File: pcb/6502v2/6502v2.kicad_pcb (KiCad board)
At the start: 2 copper layers, 119 x 119 mm, 89 parts, among them J1 Power, J10 Interup Pins, J11 I/O, J12 DB9_Female, J2 USB_C_Receptacle, J3 Barrel_Jack, J4 Conn_01x02, J5 I/O, J6 Interup Pins, J7 I/O, J8 I/O, J9 LDC, SW2 SW_Push, U1 74HC00, U2 74HC238, U3 CY62256-70PC, U4 W65C02SxP, U5 W65C22NxP, U6 W65C22NxP, U7 MAX232, U8 W65C51NxP, U9 28C256, X1 DGOF5S3, Y1 1.8432 Mh

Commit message: Laying out chips
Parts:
- moved R33 101.1 mm to (75.5, 48.0)
- moved C5 97.5 mm to (68.0, 52.0), turned to 90 degrees
- moved U2 89.4 mm to (165.4, 103.8)
- moved J6 59.7 mm to (122.4, 103.4), turned to 90 degrees
- moved U4 51.1 mm to (71.9, 107.1), turned to 180 degrees
- moved U5 49.2 mm to (134.2, 99.9), turned to 180 degrees
- moved J1 42.5 mm to (20.7, 149.6)
- moved J5 35.2 mm to (139.7, 94.5), turned to 180 degrees
- moved Y1 33.5 mm to (77.7, 52.0)
- moved U7 28.4 mm to (57.5, 47.4)
- moved J11 28.1 mm to (159.4, 88.4), turned to 180 degrees
- moved J12 24.0 mm to (45.3, 47.8)
- moved J10 20.2 mm to (151.2, 127.0)
- moved J8 16.8 mm to (153.0, 83.2), turned to 180 degrees
- moved J7 15.9 mm to (139.8, 73.3), turned to 180 degrees
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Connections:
- U2 pad 11: /Serial ~{Enable} -> /Serial Enable
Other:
- board size 119 x 119 mm -> 109 x 119 mm

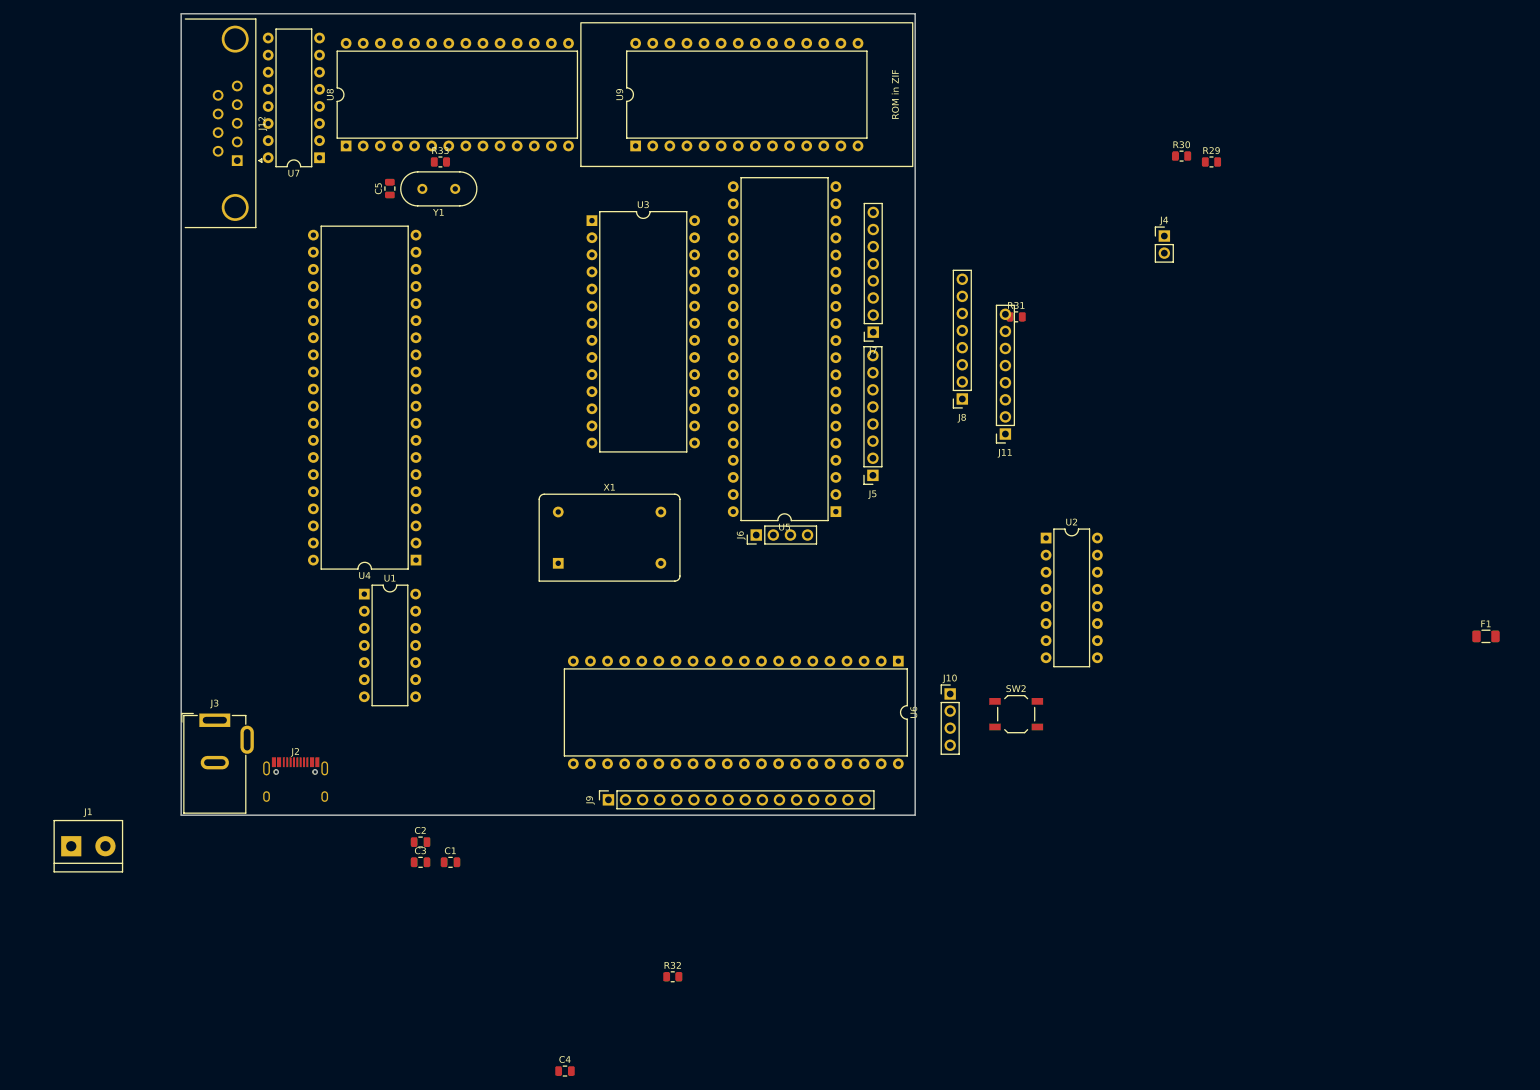
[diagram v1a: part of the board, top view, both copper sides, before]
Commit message: Yo yo yo i make the bord 102 by 102 cause jlc pricing
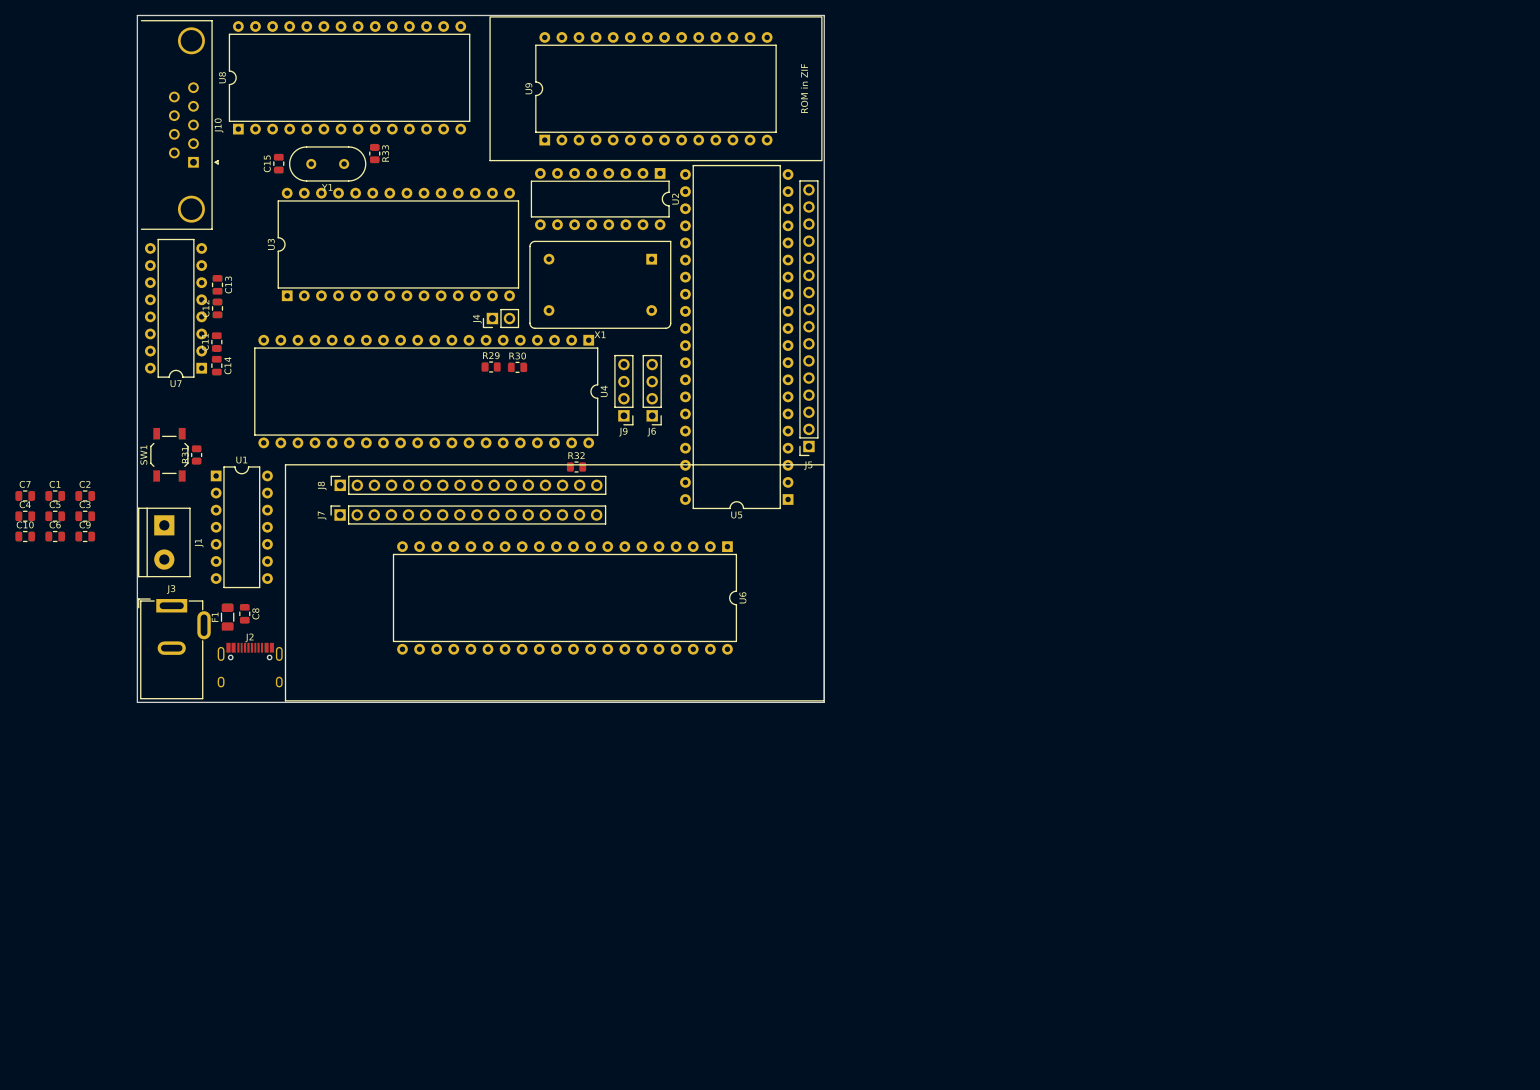
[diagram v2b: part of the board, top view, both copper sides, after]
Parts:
- removed J11: I/O, Connector_PinSocket_2.54mm:PinSocket_1x08_P2.54mm_Vertical
- removed the J8 at (153.0, 83.2)
- added C1: 10uF, Capacitor_SMD:C_0805_2012Metric, F.Cu at (18.3, 97.6)
- added C10: 10uF, Capacitor_SMD:C_0805_2012Metric, F.Cu at (13.8, 103.6)
- added C2: 10uF, Capacitor_SMD:C_0805_2012Metric, F.Cu at (22.8, 97.6)
- added C3: 10uF, Capacitor_SMD:C_0805_2012Metric, F.Cu at (22.8, 100.6)
- added C4: 10uF, Capacitor_SMD:C_0805_2012Metric, F.Cu at (13.8, 100.6)
- added C5: 10uF, Capacitor_SMD:C_0805_2012Metric, F.Cu at (18.3, 100.6)
- added C6: 10uF, Capacitor_SMD:C_0805_2012Metric, F.Cu at (18.3, 103.6)
- added C7: 10uF, Capacitor_SMD:C_0805_2012Metric, F.Cu at (13.8, 97.6)
- added C8: 10uF, Capacitor_SMD:C_0805_2012Metric, F.Cu at (46.5, 115.1)
- added C9: 10uF, Capacitor_SMD:C_0805_2012Metric, F.Cu at (22.8, 103.6)
- J5, J7: footprint Connector_PinSocket_2.54mm:PinSocket_1x08_P2.54mm_Vertical -> Connector_PinSocket_2.54mm:PinSocket_1x16_P2.54mm_Vertical
- moved F1 186.9 mm to (43.9, 115.6), turned to 90 degrees
- moved SW1 131.5 mm to (35.2, 91.5), turned to 90 degrees
- moved R31 123.4 mm to (39.3, 91.5), turned to 90 degrees
- moved C14 116.8 mm to (42.3, 78.2), turned to -90 degrees
- moved R29 111.2 mm to (83.0, 78.5)
- moved R30 103.5 mm to (87.0, 78.5)
- moved J4 100.5 mm to (83.2, 71.2), turned to 90 degrees
- moved C13 90.9 mm to (42.4, 66.2), turned to -90 degrees
- moved C12 84.8 mm to (42.4, 69.8), turned to 90 degrees
- moved C11 84.7 mm to (42.3, 74.8), turned to 90 degrees
- moved J7 83.7 mm to (60.6, 100.4), turned to 90 degrees
- moved U2 78.8 mm to (108.1, 49.7), turned to -90 degrees
- moved R32 77.0 mm to (95.7, 93.3)
- moved J9 63.7 mm to (102.8, 85.7), turned to 180 degrees
- moved J1 49.6 mm to (34.5, 102.0), turned to -90 degrees
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- renumbered C1 to C11, C2 to C12, C3 to C13, C4 to C14, C5 to C15, J12 to J10, J9 to J8, J10 to J9, SW2 to SW1
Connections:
- F1 pad 1: Net-(F1-Pad1) -> VCC
- J7 pad 1: /VIA/PB0 -> /VIA/LCD PB7
- J7 pad 2: /VIA/PB1 -> /VIA/LCD PB6
- J7 pad 3: /VIA/PB2 -> /VIA/LCD PB5
- J7 pad 4: /VIA/PB3 -> /VIA/LCD PB4
- J7 pad 5: /VIA/PB4 -> /VIA/LCD PB3
- J7 pad 6: /VIA/PB5 -> /VIA/LCD PB2
- J7 pad 7: /VIA/PB6 -> /VIA/LCD PB1
- J7 pad 8: /VIA/PB7 -> /VIA/LCD PB0
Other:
- board size 109 x 119 mm -> 102 x 102 mm
- copper layers 2 -> 4
- board text added: "We can put some SMD parts on the same side as DIP chips because of standoffs and sockets DO NOT PUT SMD PARTS ON THE ROM CHIP, THE ROM CHIP IS IN A ZIF SOCKET"

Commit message: First pass at routing done, now comes double checking everything
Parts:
- removed D11, D13, D15, D17, D18, D19, D20, D22, D23, D24, D25, D26, D3, D5, D7, D9: Red, Resistor_SMD:R_0805_2012Metric
- removed D21: Yellow, Resistor_SMD:R_0805_2012Metric
- removed J2: USB_C_Receptacle, hooks:HRO-TYPE-C-31-M-12
- removed R11, R13, R15, R17, R19, R20, R21, R22, R23, R24, R25, R26, R27, R28, R5, R7, R9: 220, Resistor_SMD:R_0805_2012Metric
- added G***: LOGO, LOGO, F.Cu at (118.0, 109.0)
- added USB1: HRO-TYPE-C-31-M-12, hooks:HRO-TYPE-C-31-M-12, F.Cu at (46.5, 128.2)
- 1.8432 Mh: renamed from Y1
- LCD Header: renamed from J8
- R10, R12, R14, R16, R18, R4, R6, R8: moved to B.Cu
- moved D10 214.4 mm to (74.5, 125.4), turned to 90 degrees
- moved R18 213.5 mm to (66.8, 125.4), turned to 90 degrees
- moved D14 210.9 mm to (69.5, 125.3), turned to 90 degrees
- moved R10 204.8 mm to (77.0, 125.3), turned to 90 degrees
- moved R2 199.9 mm to (47.6, 117.3), turned to 90 degrees
- moved R12 198.9 mm to (74.5, 125.4), turned to 90 degrees
- moved D1 198.8 mm to (48.3, 113.0), turned to 180 degrees
- moved R4 198.7 mm to (84.7, 125.3), turned to 90 degrees
- moved R1 197.3 mm to (45.6, 117.3), turned to 90 degrees
- moved D16 195.8 mm to (66.8, 125.3), turned to 90 degrees
- moved D12 195.2 mm to (72.0, 125.3), turned to 90 degrees
- moved R16 194.4 mm to (69.5, 125.3), turned to 90 degrees
- moved R3 192.2 mm to (50.8, 115.9), turned to -90 degrees
- moved D8 191.8 mm to (77.0, 125.4), turned to 90 degrees
- moved D6 190.3 mm to (79.6, 125.4), turned to 90 degrees
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- renumbered X1 to 1Mh, J3 to 5v, U4 to 65C02, U6 to 65C22, U5 to 65C22, U8 to 65C51, U1 to 74HC00, U2 to 74HC238, F1 to Fuse, J7 to GPIO, J5 to GPIO, J6 to J5, J9 to J8, J10 to J9, U7 to MAX232, J4 to NMI, U3 to RAM, SW1 to Reset
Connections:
- D1 pad 1: Net-(D1-Pad1) -> (no net)
- R3 pad 1: Net-(D1-Pad1) -> (no net)
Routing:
- net +5V: track 0.00 -> 404.8 mm, vias 0 -> 7
- net /D5: track 0.00 -> 230.1 mm, vias 0 -> 1
- net /D3: track 0.00 -> 228.8 mm, vias 0 -> 1
- net /D4: track 0.00 -> 224.8 mm
- net /I/O ~{Enable}: track 0.00 -> 223.3 mm, vias 0 -> 3
- net /D7: track 0.00 -> 219.0 mm
- net /Clk: track 0.00 -> 210.2 mm
- net /D1: track 0.00 -> 208.9 mm, vias 0 -> 1
- net /D2: track 0.00 -> 203.4 mm, vias 0 -> 1
- net /D6: track 0.00 -> 199.6 mm, vias 0 -> 1
- net /A3: track 0.00 -> 195.4 mm, vias 0 -> 1
- net /R/W: track 0.00 -> 190.8 mm, vias 0 -> 1
- net /D0: track 0.00 -> 190.8 mm, vias 0 -> 2
- net /A1: track 0.00 -> 187.0 mm, vias 0 -> 2
- net /A0: track 0.00 -> 186.0 mm
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- added copper zone on B.Cu, net GND
- added copper zone on F.Cu, net GND
- added copper zone on In1.Cu, net GND
- added copper zone on In2.Cu, net GND
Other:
- board text added: "+"
- board text added: "-"
- board text added: "Anjali <333"
- board text added: "D0"
- board text added: "D7"
- board text added: "GPIO Int Pins"
- board text added: "IRQ"
- board text added: "LCD Int Pins"
- board text added: "message = $0200 lda #%10101001 sta message lda #%00010111 sta message"
